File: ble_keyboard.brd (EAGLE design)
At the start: 70 x 35 mm, 10 parts, among them CN1 FH34SRJ-6S, CN2 FH34SRJ-10S, CN3 3711-007549, CON1 41002W90-NP-S-30

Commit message: BRD routed
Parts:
- removed CN3: 3711-007549, 3711-007549:3711-007549
- removed R3, R4: 2K, rcl:R0603
- added C1: 10nF, rcl:C0603
- added C2, C5, C7: 100n, rcl:C0603
- added C3, C6: 1uF, rcl:C0603
- added C4: 100nF, rcl:C0603
- added CIN_VIN: 53047-04, con-molex:53047-04
- added Q1: DMG6968U-7, SparkFun:SOT23-3
- added RN1: 2K, dp_devices:RN8P-4R-CRA06S
- added VREG1: MIC5200-3.3YS, dp_devices:SOT-223
- R1: value 2K -> 47K
- R2: value 2K -> 10
- U1: value (none) -> YJ-14015
- moved R1 30.8 mm to (42.4, 13.2), flipped to the top, turned to 0 degrees
- moved CN2 21.9 mm to (51.4, 21.2)
- moved CN1 21.4 mm to (42.4, 21.8)
- moved CON1 19.6 mm to (34.5, 22.9)
- moved R2 19.6 mm to (38.6, 14.5), flipped to the top, turned to 0 degrees
- moved SWD 10.6 mm to (1.75, 12.9), turned to 90 degrees
- moved U1 9.38 mm to (19.8, 13.0), flipped to the top, turned to 180 degrees
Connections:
- removed net BACKL_LED_A: CN1.1, CN1.2
- removed net BAT_DETECT: CN3.6
- removed net VBAT: CN3.1, CN3.2, CN3.3
- removed net VBAT_ADC: U1.P.01
- new net LIPO_RAW: CIN_VIN.1, CN1.1, CN1.2, VREG1.3
- new net MOTOR_A_GATE_R: Q1.1, R1.1, R2.2
- net +3V3: now also C1.1, C2.1, C3.1, C4.1, C5.1, C6.1, C7.1, VREG1.2
- net BACKLIGHT_PWM: now also R2.1
- net BACKL_LED_K: now also Q1.3
- net GND: now also C1.2, C2.2, C3.2, C4.2, C5.2, C6.2, C7.2, CIN_VIN.4, Q1.2, R1.2, VREG1.1; no longer CN3.7, CN3.8, CN3.9, CN3.MH1, CN3.MH2
- net I2C_SCL: now also CIN_VIN.3; no longer CN3.4
- net I2C_SDA: now also CIN_VIN.2; no longer CN3.5
- net KSI0: now also U1.P.25; no longer U1.P.21
- net KSI1: now also U1.P.27; no longer U1.P.22
- net KSI2: now also U1.P.28; no longer U1.P.23
- net KSI3: now also U1.P.29; no longer U1.P.24
- net KSI4: now also U1.P.30; no longer U1.P.25
- net KSI5: now also U1.P.02; no longer U1.P.26
- net KSI6: now also U1.P.04; no longer U1.P.27
- net KSI7: now also U1.P.05; no longer U1.P.28
- net KSO0: now also U1.P.21; no longer U1.P.00
- net KSO1: now also U1.P.22; no longer U1.P.30
- net KSO10: now also U1.P.09; no longer U1.P.10
- net KSO11: now also U1.P.10; no longer U1.P.11
- net KSO12: now also U1.P.11; no longer U1.P.12
- net KSO13: now also U1.P.12; no longer U1.P.13
- net KSO14: now also U1.P.13; no longer U1.P.14
- net KSO15: now also U1.P.14; no longer U1.P.15
- net KSO2: now also U1.P.23; no longer U1.P.02
- net KSO3: now also U1.P.24; no longer U1.P.03
- net KSO4: now also U1.P.26; no longer U1.P.04
- net KSO5: now also U1.P.00; no longer U1.P.05
- net KSO6: now also U1.P.03; no longer U1.P.06
- net KSO7: now also U1.P.06; no longer U1.P.07
- net KSO8: now also U1.P.07; no longer U1.P.08
- net KSO9: now also U1.P.08; no longer U1.P.09
- net LED_CAPS: now also RN1.2, U1.P.15; no longer R3.1, U1.P.19
- net LED_FN: now also RN1.1, U1.P.19; no longer R4.1, U1.P.29
- net LED_RFOFF: now also RN1.3; no longer R2.1
- net LED_TP: now also RN1.4; no longer R1.1
- net N$1: now also RN1.5; no longer R1.2
- net N$2: now also RN1.6; no longer R2.2
- net N$3: now also RN1.7; no longer R3.2
- net N$4: now also RN1.8; no longer R4.2
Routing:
- net +3V3: track 0.00 -> 75.2 mm, vias 0 -> 3
- net TOUCH_ALERT: track 0.00 -> 55.3 mm, vias 0 -> 2
- net BACKLIGHT_PWM: track 0.00 -> 54.6 mm, vias 0 -> 2
- net KSI0: track 64.4 -> 12.6 mm, vias 1 -> 0
- net GND: track 96.7 -> 139.5 mm, vias 2 -> 5
- net I2C_SCL: track 13.0 -> 50.4 mm, vias 1 -> 2
- net I2C_SDA: track 15.4 -> 52.3 mm, vias 1 -> 3
- net KSO0: track 47.6 -> 17.4 mm, vias 1 -> 0
- net KSO2: track 44.5 -> 14.8 mm, vias 1 -> 0
- net KSO3: track 42.3 -> 13.6 mm, vias 1 -> 0
- net LIPO_RAW: track 0.00 -> 24.0 mm, vias 0 -> 2
- net KSO9: track 25.7 -> 3.28 mm, vias 1 -> 0
- net KSO10: track 23.7 -> 3.32 mm, vias 1 -> 0
- net LED_FN: track 0.00 -> 16.0 mm
- net KSO1: track 0.00 -> 16.0 mm
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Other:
- board size 70 x 35 mm -> 52 x 23 mm

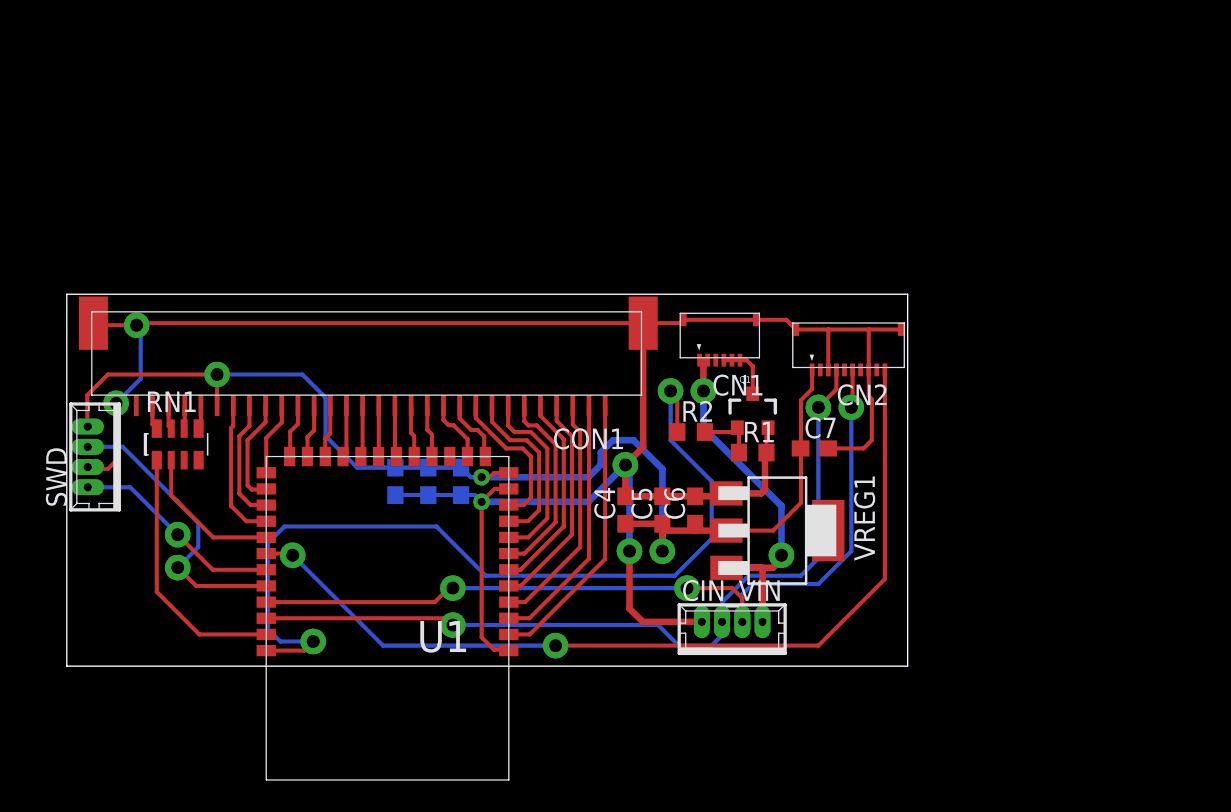
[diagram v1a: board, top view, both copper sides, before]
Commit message: - Save before BLE module rotation. - Added note abotu the best antenna gain.
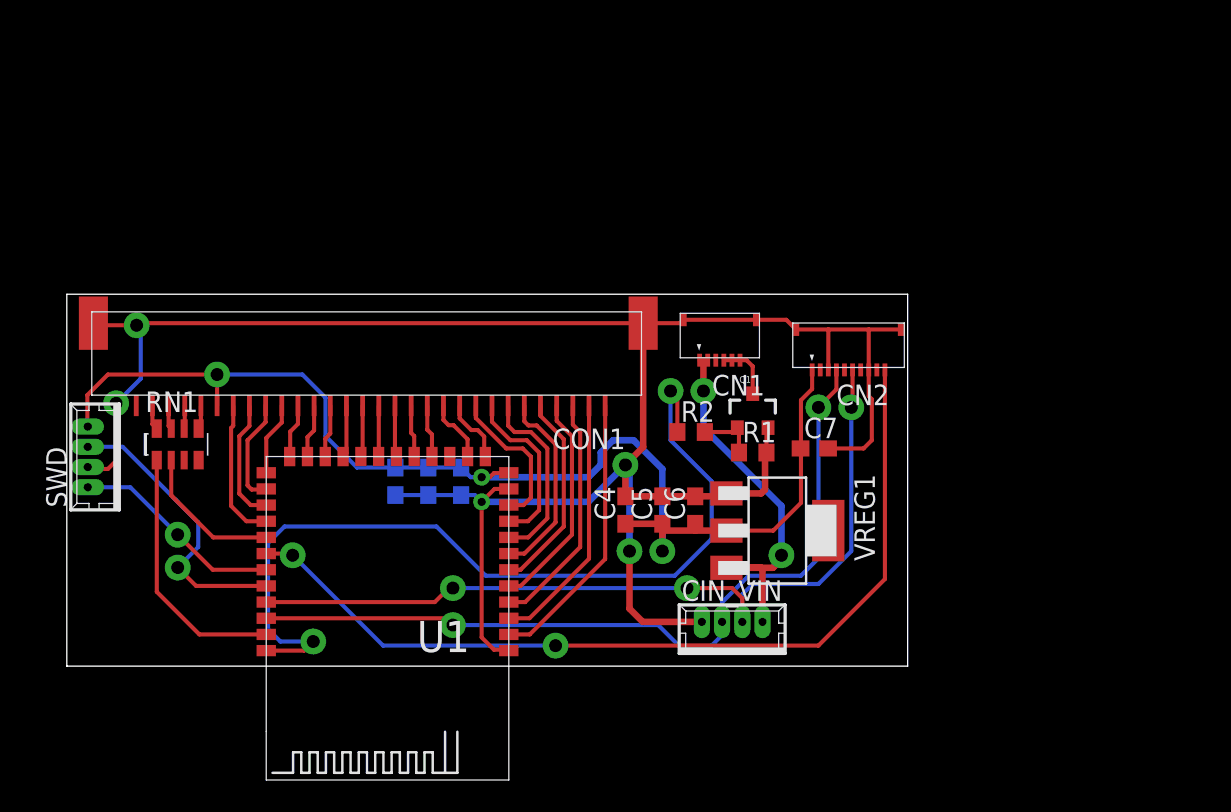
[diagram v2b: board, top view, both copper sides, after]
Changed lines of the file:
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@@
 <layer number="23" name="tOrigins" color="15" fill="1" visible="yes" active="yes"/>
 <layer number="24" name="bOrigins" color="15" fill="1" visible="yes" active="yes"/>
-<layer number="25" name="tNames" color="7" fill="1" visible="yes" active="yes"/>
-<layer number="26" name="bNames" color="7" fill="1" visible="yes" active="yes"/>
-<layer number="27" name="tValues" color="7" fill="1" visible="yes" active="yes"/>
-<layer number="28" name="bValues" color="7" fill="1" visible="yes" active="yes"/>
+<layer number="25" name="tNames" color="7" fill="1" visible="no" active="yes"/>
+<layer number="26" name="bNames" color="7" fill="1" visible="no" active="yes"/>
+<layer number="27" name="tValues" color="7" fill="1" visible="no" active="yes"/>
+<layer number="28" name="bValues" color="7" fill="1" visible="no" active="yes"/>
 <layer number="29" name="tStop" color="7" fill="3" visible="no" active="yes"/>
 <layer number="30" name="bStop" color="7" fill="6" visible="no" active="yes"/>
@@
 </autorouter>
 <elements>
-<element name="CN1" library="hirose_FH34SRJ" package="FH34SRJ-6S" value="FH34SRJ-6S" x="42.434" y="21.82" rot="R180"/>
-<element name="CN2" library="hirose_FH34SRJ" package="FH34SRJ-10S" value="FH34SRJ-10S" x="51.394" y="21.22" rot="R180"/>
-<element name="CON1" library="JTC41002" package="41200W90-NP-S" value="41002W90-NP-S-30" x="34.544" y="22.86" rot="R180"/>
-<element name="SWD" library="con-molex" package="53047-04" value="53047-04" x="1.746" y="12.938" rot="R90">
+<element name="CN1" library="hirose_FH34SRJ" package="FH34SRJ-6S" value="FH34SRJ-6S" x="42.434" y="21.82" smashed="yes" rot="R180">
+<attribute name="NAME" x="43.164" y="18.01" size="1.27" layer="25" rot="R180"/>
+<attribute name="VALUE" x="43.894" y="24.17" size="1.27" layer="27" rot="R180"/>
+</element>
+<element name="CN2" library="hirose_FH34SRJ" package="FH34SRJ-10S" value="FH34SRJ-10S" x="51.394" y="21.22" smashed="yes" rot="R180">
+<attribute name="NAME" x="50.854" y="17.41" size="1.27" layer="25" rot="R180"/>
+<attribute name="VALUE" x="50.854" y="23.57" size="1.27" layer="27" rot="R180"/>
+</element>
+<element name="CON1" library="JTC41002" package="41200W90-NP-S" value="41002W90-NP-S-30" x="34.544" y="22.86" smashed="yes" rot="R180">
+<attribute name="NAME" x="34.544" y="14.69" size="1.27" layer="25" rot="R180"/>
+<attribute name="VALUE" x="34.544" y="24.13" size="1.27" layer="27" rot="R180"/>
+</element>
+<element name="SWD" library="con-molex" package="53047-04" value="53047-04" x="1.746" y="12.938" smashed="yes" rot="R90">
 <attribute name="MF" value="WALDOM/MOLEX" x="1.746" y="12.938" size="1.778" layer="27" rot="R90" display="off"/>
 <attribute name="MPN" value="53047-0410" x="1.746" y="12.938" size="1.778" layer="27" rot="R90" display="off"/>
+<attribute name="NAME" x="-0.004" y="9.813" size="1.27" layer="25" rot="R90"/>
 <attribute name="OC_FARNELL" value="9733060" x="1.746" y="12.938" size="1.778" layer="27" rot="R90" display="off"/>
 <attribute name="OC_NEWARK" value="38C9900" x="1.746" y="12.938" size="1.778" layer="27" rot="R90" display="off"/>
-</element>
-<element name="U1" library="YJ-14015" package="YJ-14015" value="YJ-14015" x="19.834" y="12.96" rot="R180"/>
-<element name="VREG1" library="dp_devices" package="SOT-223" value=" MIC5200-3.3YS " x="43.942" y="8.382" rot="R270">
+<attribute name="VALUE" x="4.996" y="10.313" size="1.27" layer="27" rot="R90"/>
+</element>
+<element name="U1" library="YJ-14015" package="YJ-14015" value="YJ-14015" x="19.834" y="12.96" smashed="yes" rot="R180">
+<attribute name="NAME" x="24.914" y="2.8" size="1.9304" layer="25" rot="R180"/>
+<attribute name="VALUE" x="26.184" y="16.77" size="1.9304" layer="27" rot="R180"/>
+</element>
+<element name="VREG1" library="dp_devices" package="SOT-223" value=" MIC5200-3.3YS " x="43.942" y="8.382" smashed="yes" rot="R270">
+<attribute name="NAME" x="48.7045" y="11.8745" size="1.27" layer="25" font="vector" ratio="10" rot="R270"/>
 <attribute name="OC_TME" value=" MIC5200-3.3YS" x="43.942" y="8.382" size="1.778" layer="27" rot="R270" display="off"/>
-</element>
-<element name="CIN_VIN" library="con-molex" package="53047-04" value="53047-04" x="41.148" y="2.286">
+<attribute name="VALUE" x="37.9095" y="11.557" size="1.27" layer="27" font="vector" ratio="10" rot="R270"/>
+</element>
+<element name="CIN_VIN" library="con-molex" package="53047-04" value="53047-04" x="41.148" y="2.286" smashed="yes">
 <attribute name="MF" value="WALDOM/MOLEX" x="41.148" y="2.286" size="1.778" layer="27" font="vector" display="off"/>
 <attribute name="MPN" value="53047-0410" x="41.148" y="2.286" size="1.778" layer="27" font="vector" display="off"/>
+<attribute name="NAME" x="38.023" y="4.036" size="1.27" layer="25"/>
 <attribute name="OC_FARNELL" value="9733060" x="41.148" y="2.286" size="1.778" layer="27" font="vector" display="off"/>
 <attribute name="OC_NEWARK" value="38C9900" x="41.148" y="2.286" size="1.778" layer="27" font="vector" display="off"/>
-</element>
-<element name="C1" library="rcl" package="C0603" value="10nF" x="24.384" y="11.43" rot="MR270"/>
-<element name="C2" library="rcl" package="C0603" value="100n" x="22.352" y="11.43" rot="MR270"/>
-<element name="C3" library="rcl" package="C0603" value="1uF" x="20.32" y="11.43" rot="MR270"/>
-<element name="C4" library="rcl" package="C0603" value="100nF" x="34.544" y="9.652" rot="R90"/>
-<element name="C5" library="rcl" package="C0603" value="100n" x="36.83" y="9.652" rot="R90"/>
-<element name="C6" library="rcl" package="C0603" value="1uF" x="38.862" y="9.652" rot="R90"/>
-<element name="RN1" library="dp_devices" package="RN8P-4R-CRA06S" value="2K" x="6.858" y="13.716"/>
-<element name="C7" library="rcl" package="C0603" value="100n" x="46.228" y="13.462"/>
-<element name="Q1" library="SparkFun" package="SOT23-3" value="DMG6968U-7" x="42.418" y="15.748"/>
-<element name="R1" library="rcl" package="R0603" value="47K" x="42.418" y="13.208"/>
-<element name="R2" library="rcl" package="R0603" value="10" x="38.608" y="14.478"/>
+<attribute name="VALUE" x="38.523" y="-0.964" size="1.27" layer="27"/>
+</element>
+<element name="C1" library="rcl" package="C0603" value="10nF" x="24.384" y="11.43" smashed="yes" rot="MR270">
+<attribute name="NAME" x="23.749" y="12.065" size="1.27" layer="26" rot="MR270"/>
+<attribute name="VALUE" x="26.289" y="12.065" size="1.27" layer="28" rot="MR270"/>
+</element>
+<element name="C2" library="rcl" package="C0603" value="100n" x="22.352" y="11.43" smashed="yes" rot="MR270">
+<attribute name="NAME" x="21.717" y="12.065" size="1.27" layer="26" rot="MR270"/>
+<attribute name="VALUE" x="24.257" y="12.065" size="1.27" layer="28" rot="MR270"/>
+</element>
+<element name="C3" library="rcl" package="C0603" value="1uF" x="20.32" y="11.43" smashed="yes" rot="MR270">
+<attribute name="NAME" x="19.685" y="12.065" size="1.27" layer="26" rot="MR270"/>
+<attribute name="VALUE" x="22.225" y="12.065" size="1.27" layer="28" rot="MR270"/>
+</element>
+<element name="C4" library="rcl" package="C0603" value="100nF" x="34.544" y="9.652" smashed="yes" rot="R90">
+<attribute name="NAME" x="33.909" y="9.017" size="1.27" layer="25" rot="R90"/>
+<attribute name="VALUE" x="36.449" y="9.017" size="1.27" layer="27" rot="R90"/>
+</element>
+<element name="C5" library="rcl" package="C0603" value="100n" x="36.83" y="9.652" smashed="yes" rot="R90">
+<attribute name="NAME" x="36.195" y="9.017" size="1.27" layer="25" rot="R90"/>
+<attribute name="VALUE" x="38.735" y="9.017" size="1.27" layer="27" rot="R90"/>
+</element>
+<element name="C6" library="rcl" package="C0603" value="1uF" x="38.862" y="9.652" smashed="yes" rot="R90">
+<attribute name="NAME" x="38.227" y="9.017" size="1.27" layer="25" rot="R90"/>
+<attribute name="VALUE" x="40.767" y="9.017" size="1.27" layer="27" rot="R90"/>
+</element>
+<element name="RN1" library="dp_devices" package="RN8P-4R-CRA06S" value="2K" x="6.858" y="13.716" smashed="yes">
+<attribute name="NAME" x="4.858" y="15.716" size="1.27" layer="25" font="vector" ratio="10"/>
+<attribute name="VALUE" x="4.858" y="10.716" size="1.27" layer="27" font="vector" ratio="10"/>
+</element>
+<element name="C7" library="rcl" package="C0603" value="100n" x="46.228" y="13.462" smashed="yes">
+<attribute name="NAME" x="45.593" y="14.097" size="1.27" layer="25"/>
+<attribute name="VALUE" x="45.593" y="11.557" size="1.27" layer="27"/>
+</element>
+<element name="Q1" library="SparkFun" package="SOT23-3" value="DMG6968U-7" x="42.418" y="15.748" smashed="yes">
+<attribute name="NAME" x="41.5925" y="17.526" size="0.4064" layer="25"/>
+<attribute name="VALUE" x="41.402" y="15.5575" size="0.4064" layer="27"/>
+</element>
+<element name="R1" library="rcl" package="R0603" value="47K" x="42.418" y="13.208" smashed="yes">
+<attribute name="NAME" x="41.783" y="13.843" size="1.27" layer="25"/>
+<attribute name="VALUE" x="41.783" y="11.303" size="1.27" layer="27"/>
+</element>
+<element name="R2" library="rcl" package="R0603" value="10" x="38.608" y="14.478" smashed="yes">
+<attribute name="NAME" x="37.973" y="15.113" size="1.27" layer="25"/>
+<attribute name="VALUE" x="37.973" y="12.573" size="1.27" layer="27"/>
+</element>
 </elements>
 <signals>
